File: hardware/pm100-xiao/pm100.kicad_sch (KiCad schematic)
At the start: 42 parts, among them J1 VCC-BATT, J10 NRST, J2 VCC-ESC, J4 GND-BATT, J5 UART, J6 RECEIVER, J7 ESC, J8 SWDIO, J9 SWCLK, Q5 BSS138, Q6 BSS138, Q7 BSS138, Q8 BSS138, SW1 CLASSE, SW3 Reset, U3 LD1117S50TR_SOT223, U8 INA226

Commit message: first release version
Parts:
- removed C6: 0.1u, Capacitor_SMD:C_0603_1608Metric, symbol Device:C_Small
- removed J10: NRST, TestPoint:TestPoint_Pad_D2.0mm, symbol Connector_Generic:Conn_01x01
- removed J8: SWDIO, TestPoint:TestPoint_Pad_D2.0mm, symbol Connector_Generic:Conn_01x01
- removed J9: SWCLK, TestPoint:TestPoint_Pad_D2.0mm, symbol Connector_Generic:Conn_01x01
- removed SW3: Reset, Button_Switch_SMD:SW_SPST_B3U-3100P-B, symbol Switch:SW_Push
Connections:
- net LED: now also U1.18 (DIO); no longer U1.11 (MOSI/P1.15)
- net RST: no longer names the net of U1.17 (RST)

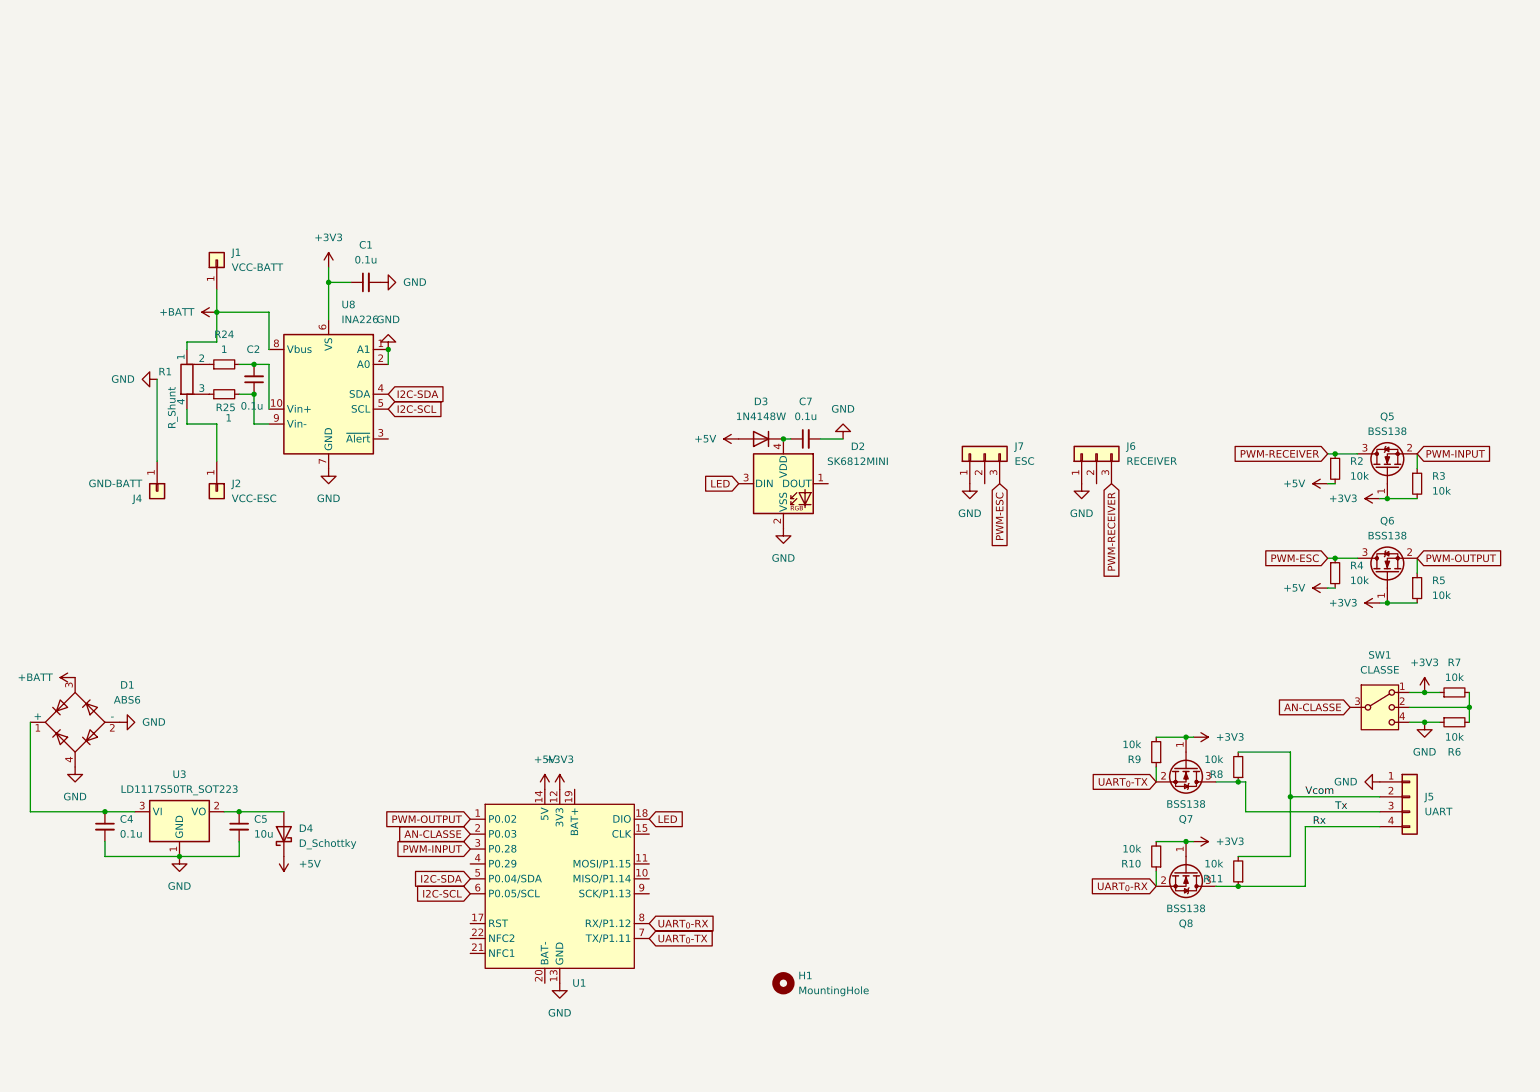
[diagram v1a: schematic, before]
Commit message: atualizando fonte e adicionado entrada auxiliar para desligar controle
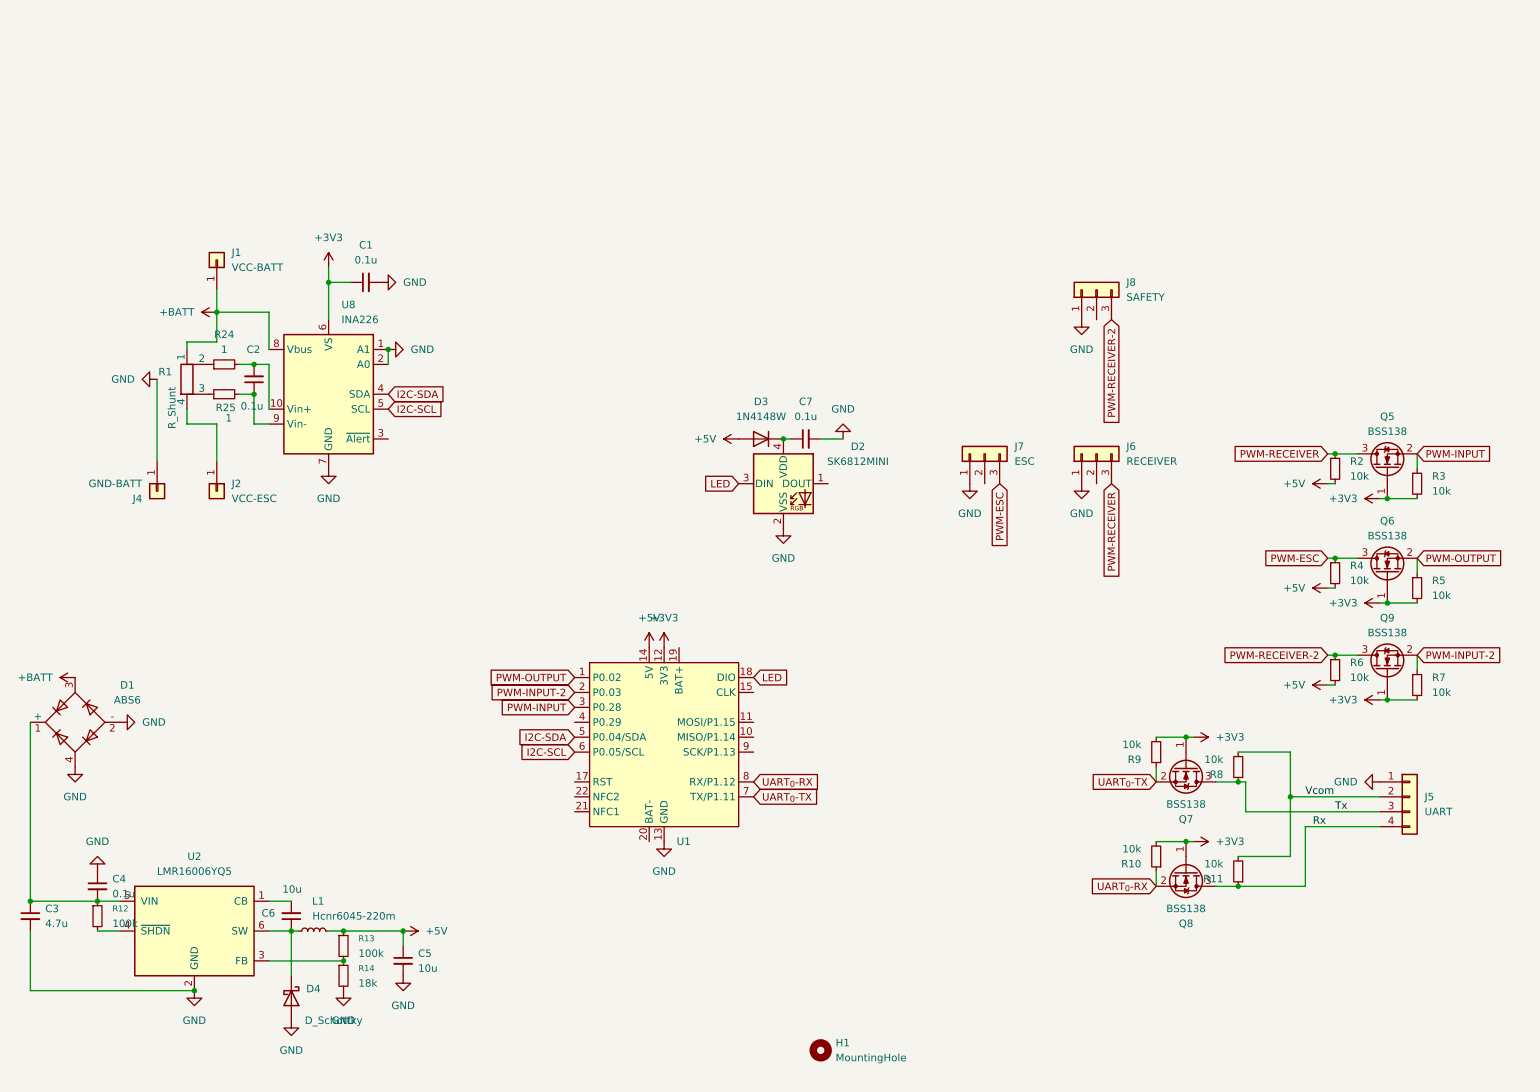
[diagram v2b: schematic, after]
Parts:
- removed SW1: CLASSE, Button_Switch_SMD:SW_SP3T_PCM13, symbol Switch:SW_SP3T
- removed U3: LD1117S50TR_SOT223, Package_TO_SOT_SMD:SOT-223-3_TabPin2, symbol Regulator_Linear:LD1117S50TR_SOT223
- added C4: 0.1u, Capacitor_SMD:C_0805_2012Metric, symbol Device:C_Small
- added C6: 10u, Capacitor_SMD:C_0805_2012Metric, symbol Device:C_Small
- added J8: SAFETY, Sigma Footprints:SolderWire_SMD_3, symbol Connector_Generic:Conn_01x03
- added L1: Hcnr6045-220m, Inductor_SMD:L_Bourns_SRN6045TA, symbol Device:L_Small
- added Q9: BSS138, Package_TO_SOT_SMD:SOT-23, symbol Transistor_FET:BSS138
- added R12, R13: 100k, Resistor_SMD:R_0603_1608Metric, symbol Device:R_Small
- added R14: 18k, Resistor_SMD:R_0603_1608Metric, symbol Device:R_Small
- added U2: LMR16006YQ5, Package_TO_SOT_SMD:SOT-23-6, symbol Regulator_Switching:LMR16006YQ5
- C3: renamed from C4; value 0.1u -> 4.7u; footprint Capacitor_SMD:C_0603_1608Metric -> Capacitor_SMD:C_0805_2012Metric
- U1: value ~ -> (none)
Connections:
- net +3V3: now also R7.2, Q9.1 (G); no longer R7.1
- net +5V: now also C5.1, R6.2, L1.2, R13.1; no longer D4.1 (K)
- net GND: now also D4.2 (A), C4.1, J8.1 (Pin_1), R14.2, U2.2 (GND); no longer R6.1
- net at C3.1, D1.1 (+): now also C4.2, R12.1, U2.5 (VIN)
- net AN-CLASSE renamed PWM-INPUT-2
- net PWM-INPUT-2: now also R7.1, Q9.2 (S)
- new net: C6.1, D4.1 (K), L1.1, U2.6 (SW)
- new net: R12.2, U2.4 (~{SHDN})
- new net: C6.2, U2.1 (CB)
- new net: R13.2, R14.1, U2.3 (FB)
- new net PWM-RECEIVER-2: J8.3 (Pin_3), Q9.3 (D), R6.1
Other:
- moved on the sheet: C3, C5, D4, H1, U1

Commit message: rev4 projeto eletronico
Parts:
- removed J1: VCC-BATT, footprints:HV_CONN_01x01_pad_6.2x12mm, symbol Connector_Generic:Conn_01x01
- removed J2: VCC-ESC, footprints:HV_CONN_01x01_pad_6.2x12mm, symbol Connector_Generic:Conn_01x01
- removed J4: GND-BATT, footprints:HV_CONN_01x01_pad_6.2x12mm, symbol Connector_Generic:Conn_01x01
- added J2: HV-BATTERY, Connector_AMASS:AMASS_XT60IPW-M_1x03_P7.20mm_Horizontal, symbol Connector_Generic:Conn_01x02
- added J3: HV-ESC, Connector_AMASS:AMASS_XT60PW-F_1x02_P7.20mm_Horizontal, symbol Connector_Generic:Conn_01x02
- D4: value D_Schottky -> SS18
- J5: footprint Connector_JST:JST_XH_S4B-XH-A-1_1x04_P2.50mm_Horizontal -> Connector_Hirose:Hirose_DF13-04P-1.25DS_1x04_P1.25mm_Horizontal
- J6, J7, J8: footprint Sigma Footprints:SolderWire_SMD_3 -> pm100:smd-pwm-3-Wire
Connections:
- net +BATT: now also R1.4, J2.2 (Pin_2); no longer R1.1
- net GND: now also J2.1 (Pin_1), J3.1 (Pin_1)
- net LED: now also U1.11 (MOSI/P1.15); no longer U1.18 (DIO)
- net at R24.1: now also R1.3; no longer R1.2
- net at R25.1: now also R1.2; no longer R1.3
- new net: J3.2 (Pin_2), R1.1
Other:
- moved on the sheet: C1, C2, C3, C4, C5, C6, C7, D1, D2, D3, D4, J6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
